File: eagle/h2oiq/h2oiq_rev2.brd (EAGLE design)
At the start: 41.3 x 64.1 mm, 25 parts, among them T1 Darlington, T2 BC846

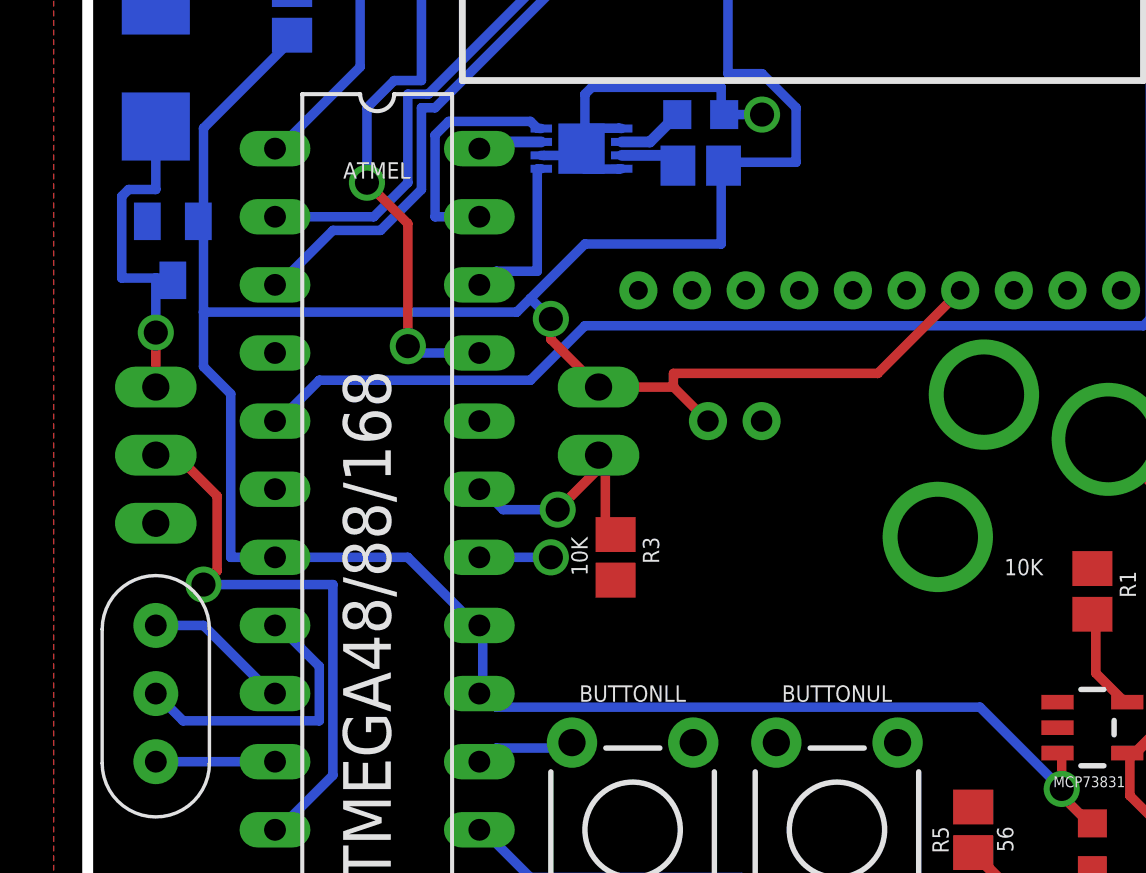
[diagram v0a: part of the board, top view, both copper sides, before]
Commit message: Minor board change for the LPFK
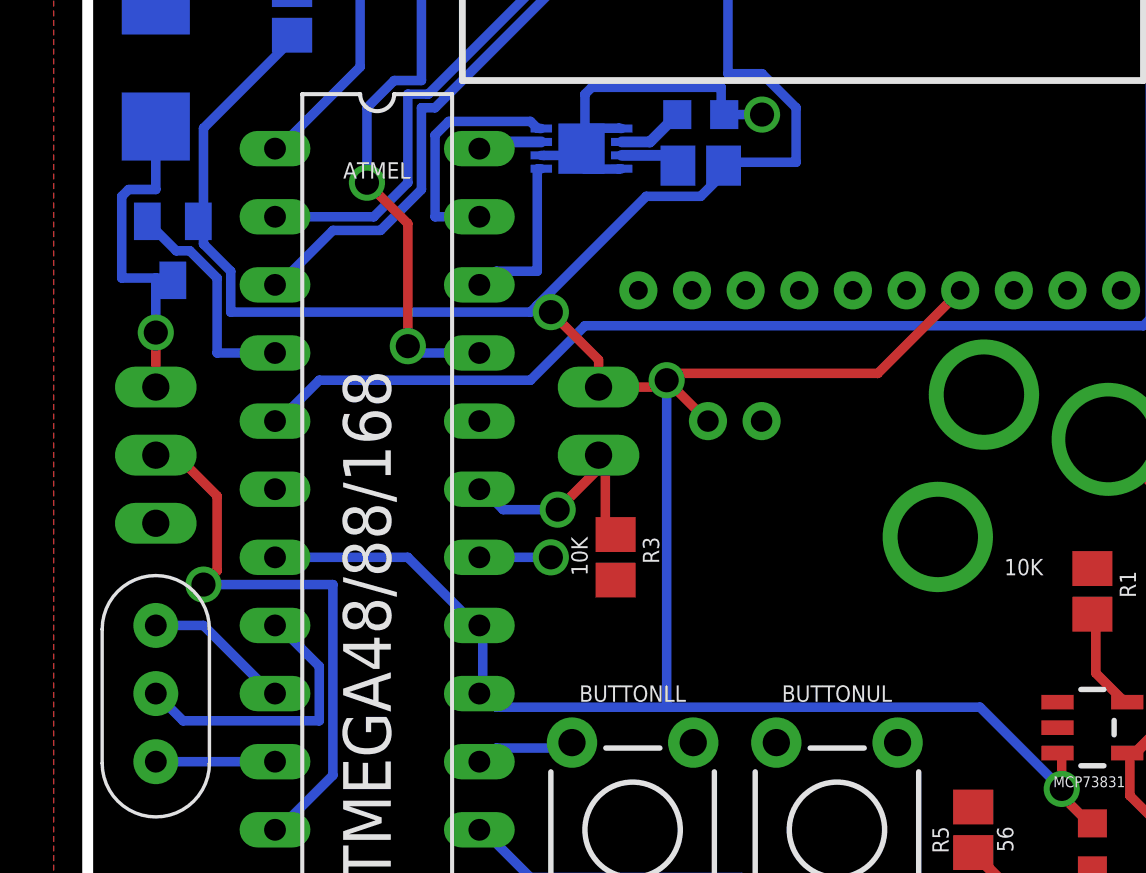
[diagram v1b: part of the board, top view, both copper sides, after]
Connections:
- net SERVOON: now also ATMEL.4
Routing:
- net SERVOON: track 0.00 -> 8.44 mm
- net VCC: track 128.8 -> 127.9 mm, vias 3 -> 4
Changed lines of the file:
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@@
 <wire x1="6.985" y1="25.4" x2="11.938" y2="25.4" width="0.3556" layer="16"/>
 <wire x1="14.478" y1="22.86" x2="14.605" y2="22.86" width="0.3556" layer="16"/>
-<wire x1="4.318" y1="32.512" x2="4.318" y2="34.544" width="0.3556" layer="16"/>
-<wire x1="4.318" y1="34.544" x2="4.318" y2="37.846" width="0.3556" layer="16"/>
-<wire x1="5.334" y1="31.496" x2="4.318" y2="32.512" width="0.3556" layer="16"/>
-<wire x1="5.334" y1="25.4" x2="5.334" y2="31.496" width="0.3556" layer="16"/>
-<wire x1="6.985" y1="25.4" x2="5.334" y2="25.4" width="0.3556" layer="16"/>
-<wire x1="4.318" y1="37.846" x2="4.125" y2="37.93" width="0.3556" layer="16"/>
 <contactref element="JP4" pad="2"/>
-<wire x1="23.622" y1="37.084" x2="23.622" y2="39.878" width="0.3556" layer="16"/>
-<wire x1="18.542" y1="37.084" x2="23.622" y2="37.084" width="0.3556" layer="16"/>
-<wire x1="16.002" y1="34.544" x2="16.51" y2="35.052" width="0.3556" layer="16"/>
-<wire x1="16.51" y1="35.052" x2="18.542" y2="37.084" width="0.3556" layer="16"/>
-<wire x1="4.318" y1="34.544" x2="16.002" y2="34.544" width="0.3556" layer="16"/>
-<wire x1="23.622" y1="39.878" x2="23.71" y2="40.005" width="0.3556" layer="16"/>
 <wire x1="4.318" y1="41.402" x2="7.62" y2="44.704" width="0.3556" layer="16"/>
 <wire x1="4.318" y1="38.1" x2="4.318" y2="41.402" width="0.3556" layer="16"/>
@@
 <via x="23.876" y="51.562" extent="1-16" drill="0.899159375"/>
 <wire x1="21.844" y1="31.75" x2="23.114" y2="30.48" width="0.3556" layer="1"/>
-<wire x1="19.05" y1="31.75" x2="21.844" y2="31.75" width="0.3556" layer="1"/>
+<wire x1="19.05" y1="31.75" x2="21.59" y2="31.75" width="0.3556" layer="1"/>
+<wire x1="21.59" y1="31.75" x2="21.844" y2="31.75" width="0.3556" layer="1"/>
 <wire x1="23.114" y1="30.48" x2="23.13" y2="30.48" width="0.3556" layer="1"/>
 <wire x1="29.464" y1="32.258" x2="32.512" y2="35.306" width="0.3556" layer="1"/>
@@
 <wire x1="21.844" y1="31.75" x2="21.844" y2="32.258" width="0.3556" layer="1"/>
 <wire x1="32.512" y1="35.306" x2="32.535" y2="35.355" width="0.3556" layer="1"/>
-<wire x1="17.272" y1="33.528" x2="19.05" y2="31.75" width="0.3556" layer="1"/>
-<wire x1="17.272" y1="34.29" x2="17.272" y2="33.528" width="0.3556" layer="1"/>
-<wire x1="16.51" y1="35.052" x2="17.272" y2="34.29" width="0.3556" layer="16"/>
 <wire x1="36.322" y1="16.51" x2="37.338" y2="15.494" width="0.3556" layer="1"/>
 <wire x1="36.322" y1="18.034" x2="36.322" y2="16.764" width="0.3556" layer="1"/>
@@
 <wire x1="36.322" y1="18.034" x2="36.1649" y2="18.1" width="0.3556" layer="1"/>
 <wire x1="33.274" y1="19.812" x2="36.322" y2="16.764" width="0.3556" layer="16"/>
-<wire x1="15.24" y1="19.812" x2="33.274" y2="19.812" width="0.3556" layer="16"/>
+<wire x1="15.24" y1="19.812" x2="21.59" y2="19.812" width="0.3556" layer="16"/>
+<wire x1="21.59" y1="19.812" x2="33.274" y2="19.812" width="0.3556" layer="16"/>
 <wire x1="14.732" y1="20.32" x2="15.24" y2="19.812" width="0.3556" layer="16"/>
 <wire x1="14.732" y1="20.32" x2="14.732" y2="22.86" width="0.3556" layer="16"/>
 <wire x1="14.732" y1="22.86" x2="14.605" y2="22.86" width="0.3556" layer="16"/>
 <wire x1="14.732" y1="20.32" x2="14.605" y2="20.32" width="0.3556" layer="16"/>
-<via x="17.272" y="34.29" extent="1-16" drill="0.899159375"/>
 <via x="36.322" y="16.764" extent="1-16" drill="0.899159375"/>
+<wire x1="4.318" y1="37.084" x2="4.318" y2="37.846" width="0.3556" layer="16"/>
+<wire x1="5.334" y1="36.068" x2="4.318" y2="37.084" width="0.3556" layer="16"/>
+<wire x1="5.334" y1="34.544" x2="5.334" y2="36.068" width="0.3556" layer="16"/>
+<wire x1="16.51" y1="34.544" x2="5.334" y2="34.544" width="0.3556" layer="16"/>
+<wire x1="20.828" y1="38.862" x2="16.764" y2="34.798" width="0.3556" layer="16"/>
+<wire x1="16.764" y1="34.798" x2="16.51" y2="34.544" width="0.3556" layer="16"/>
+<wire x1="22.86" y1="38.862" x2="20.828" y2="38.862" width="0.3556" layer="16"/>
+<wire x1="23.876" y1="39.878" x2="22.86" y2="38.862" width="0.3556" layer="16"/>
+<wire x1="4.318" y1="37.846" x2="4.125" y2="37.93" width="0.3556" layer="16"/>
+<wire x1="23.876" y1="39.878" x2="23.71" y2="40.005" width="0.3556" layer="16"/>
+<wire x1="17.018" y1="34.544" x2="16.764" y2="34.798" width="0.3556" layer="16"/>
+<wire x1="17.272" y1="34.544" x2="17.018" y2="34.544" width="0.3556" layer="16"/>
+<wire x1="19.05" y1="32.766" x2="17.272" y2="34.544" width="0.3556" layer="1"/>
+<wire x1="19.05" y1="31.75" x2="19.05" y2="32.766" width="0.3556" layer="1"/>
+<wire x1="21.59" y1="32.004" x2="21.59" y2="31.75" width="0.3556" layer="1"/>
+<wire x1="21.59" y1="19.812" x2="21.59" y2="32.004" width="0.3556" layer="16"/>
+<via x="17.272" y="34.544" extent="1-16" drill="0.899159375"/>
+<via x="21.59" y="32.004" extent="1-16" drill="0.899159375"/>
 </signal>
 <signal name="N$2">
@@
 <signal name="SERVOON">
 <contactref element="T1" pad="B"/>
+<contactref element="ATMEL" pad="4"/>
+<wire x1="3.302" y1="36.83" x2="2.286" y2="37.846" width="0.3556" layer="16"/>
+<wire x1="3.81" y1="36.83" x2="3.302" y2="36.83" width="0.3556" layer="16"/>
+<wire x1="4.826" y1="35.814" x2="3.81" y2="36.83" width="0.3556" layer="16"/>
+<wire x1="4.826" y1="33.02" x2="4.826" y2="35.814" width="0.3556" layer="16"/>
+<wire x1="6.985" y1="33.02" x2="4.826" y2="33.02" width="0.3556" layer="16"/>
+<wire x1="2.286" y1="37.846" x2="2.225" y2="37.93" width="0.3556" layer="16"/>
 </signal>
 <signal name="MOISTUREVCC">

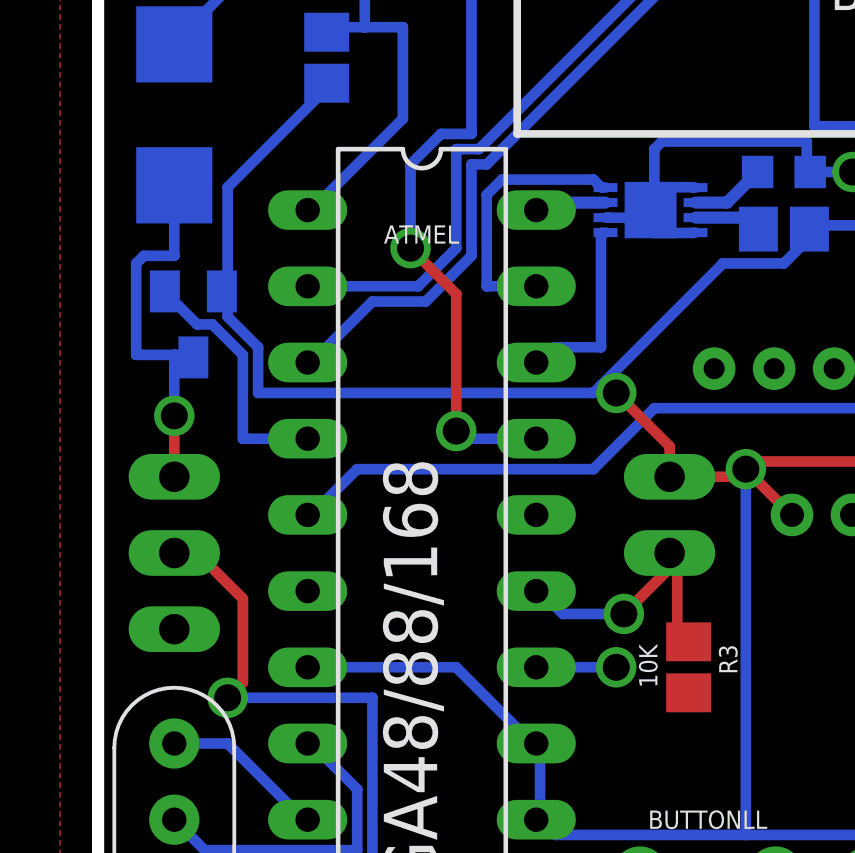
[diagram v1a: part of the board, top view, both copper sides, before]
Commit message: Adding Demo Arduino Code, as well as updated board changes
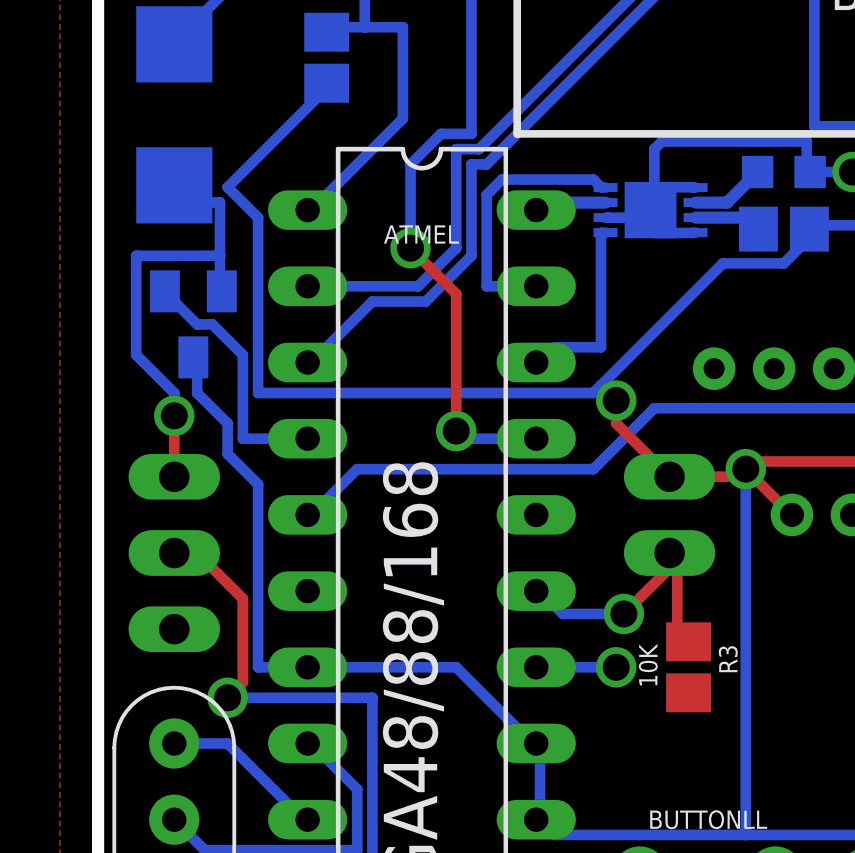
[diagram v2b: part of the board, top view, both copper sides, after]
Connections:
- net SERVOACT: now also T1.E; no longer T1.C
- net VCC: now also T1.C; no longer T1.E
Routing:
- net VCC: track 127.9 -> 140.4 mm
- net SERVOACT: track 13.0 -> 15.5 mm
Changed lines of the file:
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@@
 <contactref element="C3" pad="1"/>
 <contactref element="R2" pad="2"/>
-<contactref element="T1" pad="E"/>
 <contactref element="ATMEL" pad="20"/>
 <contactref element="XBEE" pad="1"/>
@@
 <contactref element="JP4" pad="2"/>
 <wire x1="4.318" y1="41.402" x2="7.62" y2="44.704" width="0.3556" layer="16"/>
-<wire x1="4.318" y1="38.1" x2="4.318" y2="41.402" width="0.3556" layer="16"/>
 <wire x1="7.62" y1="44.704" x2="7.62" y2="44.87" width="0.3556" layer="16"/>
-<wire x1="4.318" y1="38.1" x2="4.125" y2="37.93" width="0.3556" layer="16"/>
 <wire x1="20.828" y1="56.896" x2="20.574" y2="57.15" width="0.3556" layer="1"/>
 <wire x1="20.828" y1="54.61" x2="20.828" y2="56.896" width="0.3556" layer="1"/>
@@
 <wire x1="14.732" y1="20.32" x2="14.605" y2="20.32" width="0.3556" layer="16"/>
 <via x="36.322" y="16.764" extent="1-16" drill="0.899159375"/>
-<wire x1="4.318" y1="37.084" x2="4.318" y2="37.846" width="0.3556" layer="16"/>
-<wire x1="5.334" y1="36.068" x2="4.318" y2="37.084" width="0.3556" layer="16"/>
-<wire x1="5.334" y1="34.544" x2="5.334" y2="36.068" width="0.3556" layer="16"/>
+<wire x1="21.59" y1="32.004" x2="21.59" y2="31.75" width="0.3556" layer="1"/>
+<wire x1="21.59" y1="19.812" x2="21.59" y2="32.004" width="0.3556" layer="16"/>
+<via x="21.59" y="32.004" extent="1-16" drill="0.899159375"/>
+<contactref element="T1" pad="C"/>
+<wire x1="3.302" y1="34.544" x2="3.302" y2="35.56" width="0.3556" layer="16"/>
+<wire x1="4.318" y1="33.528" x2="3.302" y2="34.544" width="0.3556" layer="16"/>
+<wire x1="4.318" y1="32.512" x2="4.318" y2="33.528" width="0.3556" layer="16"/>
+<wire x1="5.334" y1="31.496" x2="4.318" y2="32.512" width="0.3556" layer="16"/>
+<wire x1="5.334" y1="25.4" x2="5.334" y2="31.496" width="0.3556" layer="16"/>
+<wire x1="6.985" y1="25.4" x2="5.334" y2="25.4" width="0.3556" layer="16"/>
+<wire x1="3.302" y1="35.56" x2="3.175" y2="35.73" width="0.3556" layer="16"/>
+<wire x1="5.334" y1="40.386" x2="4.318" y2="41.402" width="0.3556" layer="16"/>
+<wire x1="5.334" y1="34.544" x2="5.334" y2="40.386" width="0.3556" layer="16"/>
 <wire x1="16.51" y1="34.544" x2="5.334" y2="34.544" width="0.3556" layer="16"/>
 <wire x1="20.828" y1="38.862" x2="16.764" y2="34.798" width="0.3556" layer="16"/>
@@
 <wire x1="22.86" y1="38.862" x2="20.828" y2="38.862" width="0.3556" layer="16"/>
 <wire x1="23.876" y1="39.878" x2="22.86" y2="38.862" width="0.3556" layer="16"/>
-<wire x1="4.318" y1="37.846" x2="4.125" y2="37.93" width="0.3556" layer="16"/>
 <wire x1="23.876" y1="39.878" x2="23.71" y2="40.005" width="0.3556" layer="16"/>
-<wire x1="17.018" y1="34.544" x2="16.764" y2="34.798" width="0.3556" layer="16"/>
-<wire x1="17.272" y1="34.544" x2="17.018" y2="34.544" width="0.3556" layer="16"/>
-<wire x1="19.05" y1="32.766" x2="17.272" y2="34.544" width="0.3556" layer="1"/>
-<wire x1="19.05" y1="31.75" x2="19.05" y2="32.766" width="0.3556" layer="1"/>
-<wire x1="21.59" y1="32.004" x2="21.59" y2="31.75" width="0.3556" layer="1"/>
-<wire x1="21.59" y1="19.812" x2="21.59" y2="32.004" width="0.3556" layer="16"/>
-<via x="17.272" y="34.544" extent="1-16" drill="0.899159375"/>
-<via x="21.59" y="32.004" extent="1-16" drill="0.899159375"/>
+<wire x1="17.272" y1="33.528" x2="19.05" y2="31.75" width="0.3556" layer="1"/>
+<wire x1="17.272" y1="34.29" x2="17.272" y2="33.528" width="0.3556" layer="1"/>
+<wire x1="16.764" y1="34.798" x2="17.272" y2="34.29" width="0.3556" layer="16"/>
+<via x="17.272" y="34.29" extent="1-16" drill="0.899159375"/>
 </signal>
 <signal name="N$2">
@@
 </signal>
 <signal name="SERVOACT">
-<contactref element="T1" pad="C"/>
 <contactref element="JP2" pad="3"/>
 <contactref element="D1" pad="C"/>
-<wire x1="3.048" y1="35.56" x2="3.175" y2="35.73" width="0.3556" layer="16"/>
-<wire x1="2.54" y1="39.116" x2="2.54" y2="41.4655" width="0.3556" layer="16"/>
-<wire x1="1.524" y1="39.116" x2="2.54" y2="39.116" width="0.3556" layer="16"/>
-<wire x1="1.27" y1="38.862" x2="1.524" y2="39.116" width="0.3556" layer="16"/>
-<wire x1="1.27" y1="35.814" x2="1.27" y2="38.862" width="0.3556" layer="16"/>
-<wire x1="3.048" y1="35.814" x2="2.54" y2="35.814" width="0.3556" layer="16"/>
-<wire x1="2.54" y1="35.814" x2="1.27" y2="35.814" width="0.3556" layer="16"/>
-<wire x1="3.048" y1="35.814" x2="3.175" y2="35.73" width="0.3556" layer="16"/>
 <wire x1="2.54" y1="33.782" x2="2.54" y2="31.75" width="0.3556" layer="1"/>
-<wire x1="2.54" y1="35.814" x2="2.54" y2="33.782" width="0.3556" layer="16"/>
 <via x="2.54" y="33.782" extent="1-16" drill="0.899159375"/>
+<contactref element="T1" pad="E"/>
+<wire x1="4.064" y1="40.894" x2="4.064" y2="39.116" width="0.3556" layer="16"/>
+<wire x1="4.064" y1="39.116" x2="4.064" y2="38.1" width="0.3556" layer="16"/>
+<wire x1="3.048" y1="40.894" x2="4.064" y2="40.894" width="0.3556" layer="16"/>
+<wire x1="2.54" y1="41.402" x2="3.048" y2="40.894" width="0.3556" layer="16"/>
+<wire x1="4.064" y1="38.1" x2="4.125" y2="37.93" width="0.3556" layer="16"/>
+<wire x1="2.54" y1="41.402" x2="2.54" y2="41.4655" width="0.3556" layer="16"/>
+<wire x1="2.54" y1="34.544" x2="2.54" y2="33.782" width="0.3556" layer="16"/>
+<wire x1="1.27" y1="35.814" x2="2.54" y2="34.544" width="0.3556" layer="16"/>
+<wire x1="1.27" y1="39.116" x2="1.27" y2="35.814" width="0.3556" layer="16"/>
+<wire x1="4.064" y1="39.116" x2="1.27" y2="39.116" width="0.3556" layer="16"/>
 </signal>
 <signal name="N$21">
@@
 </signal>
 </signals>
-<errors>
-</errors>
 </board>
 </drawing>
